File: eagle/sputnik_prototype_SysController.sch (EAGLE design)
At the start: 23 parts, among them U1 MEGA128-M, U2 MIC5219 3.3V, Y2 8MHZ

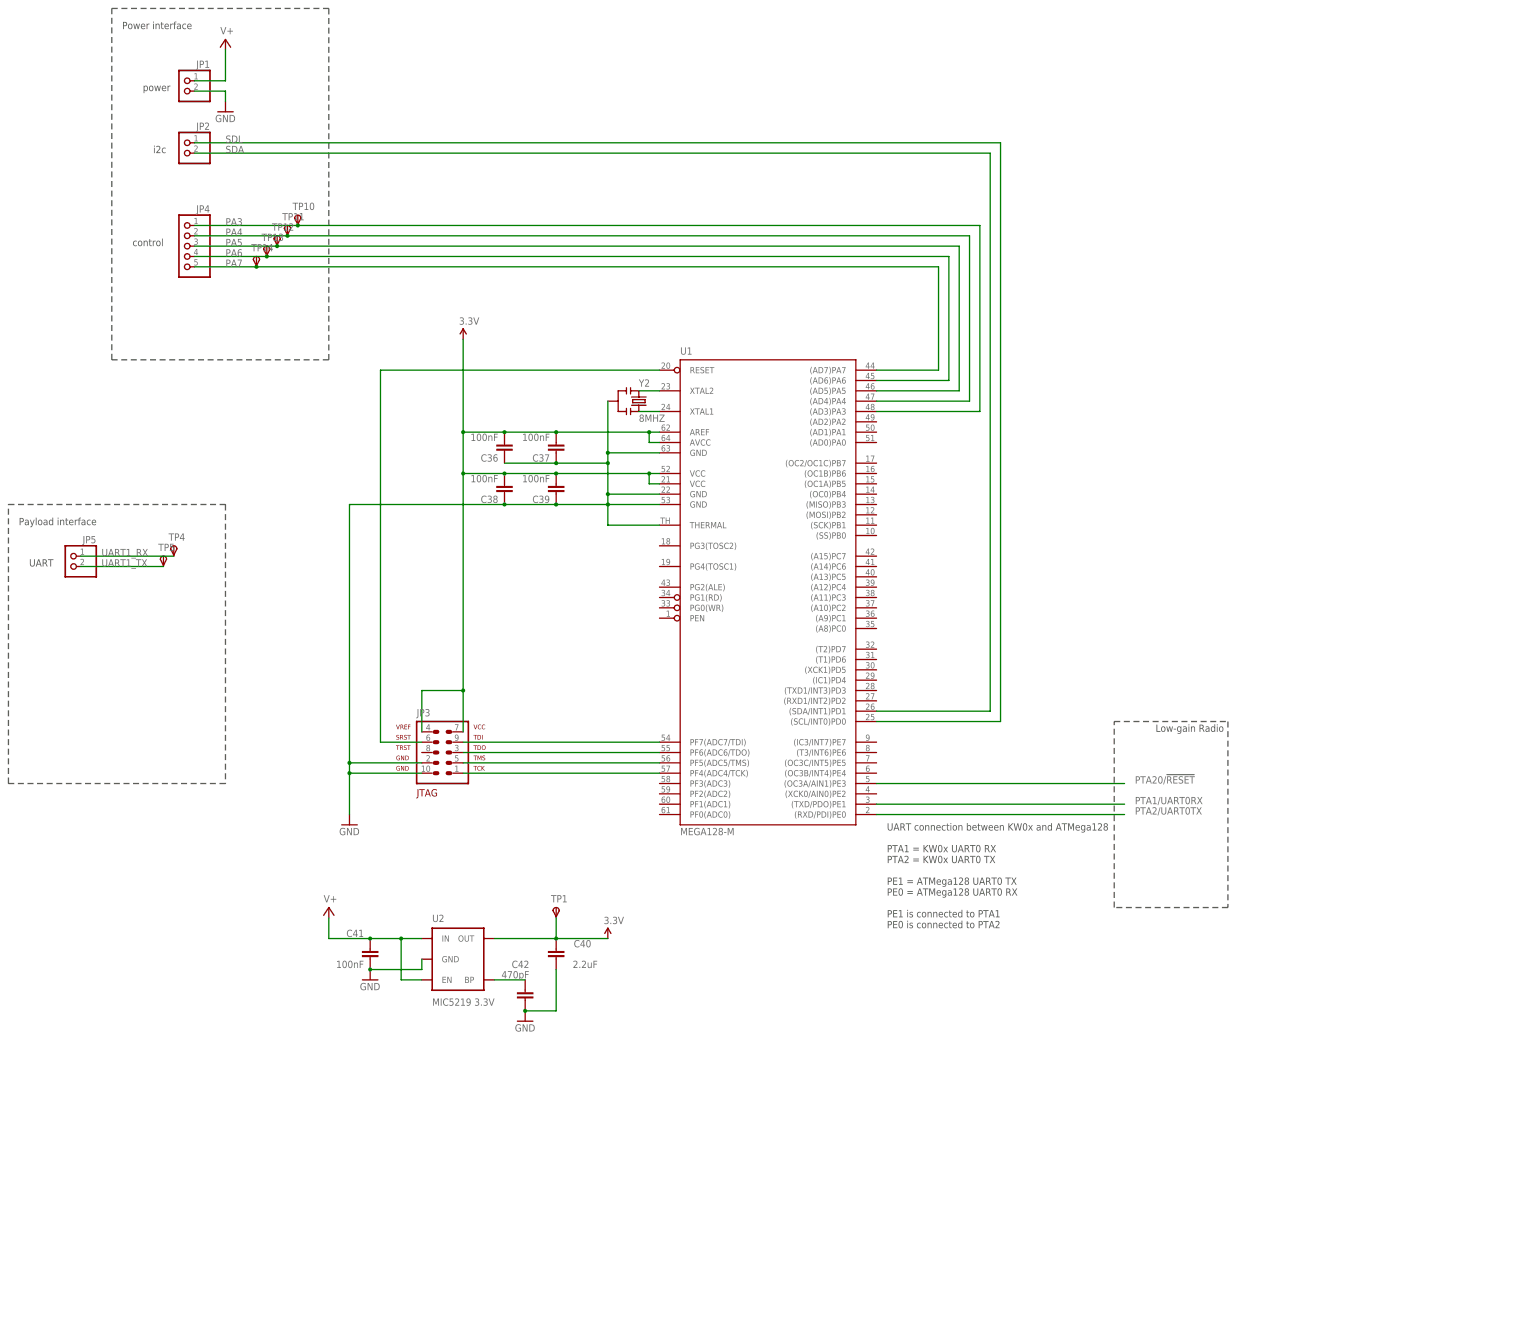
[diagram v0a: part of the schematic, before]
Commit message: Added GPIOs and other updates on SysCon sch. Updated SPI cache footprint
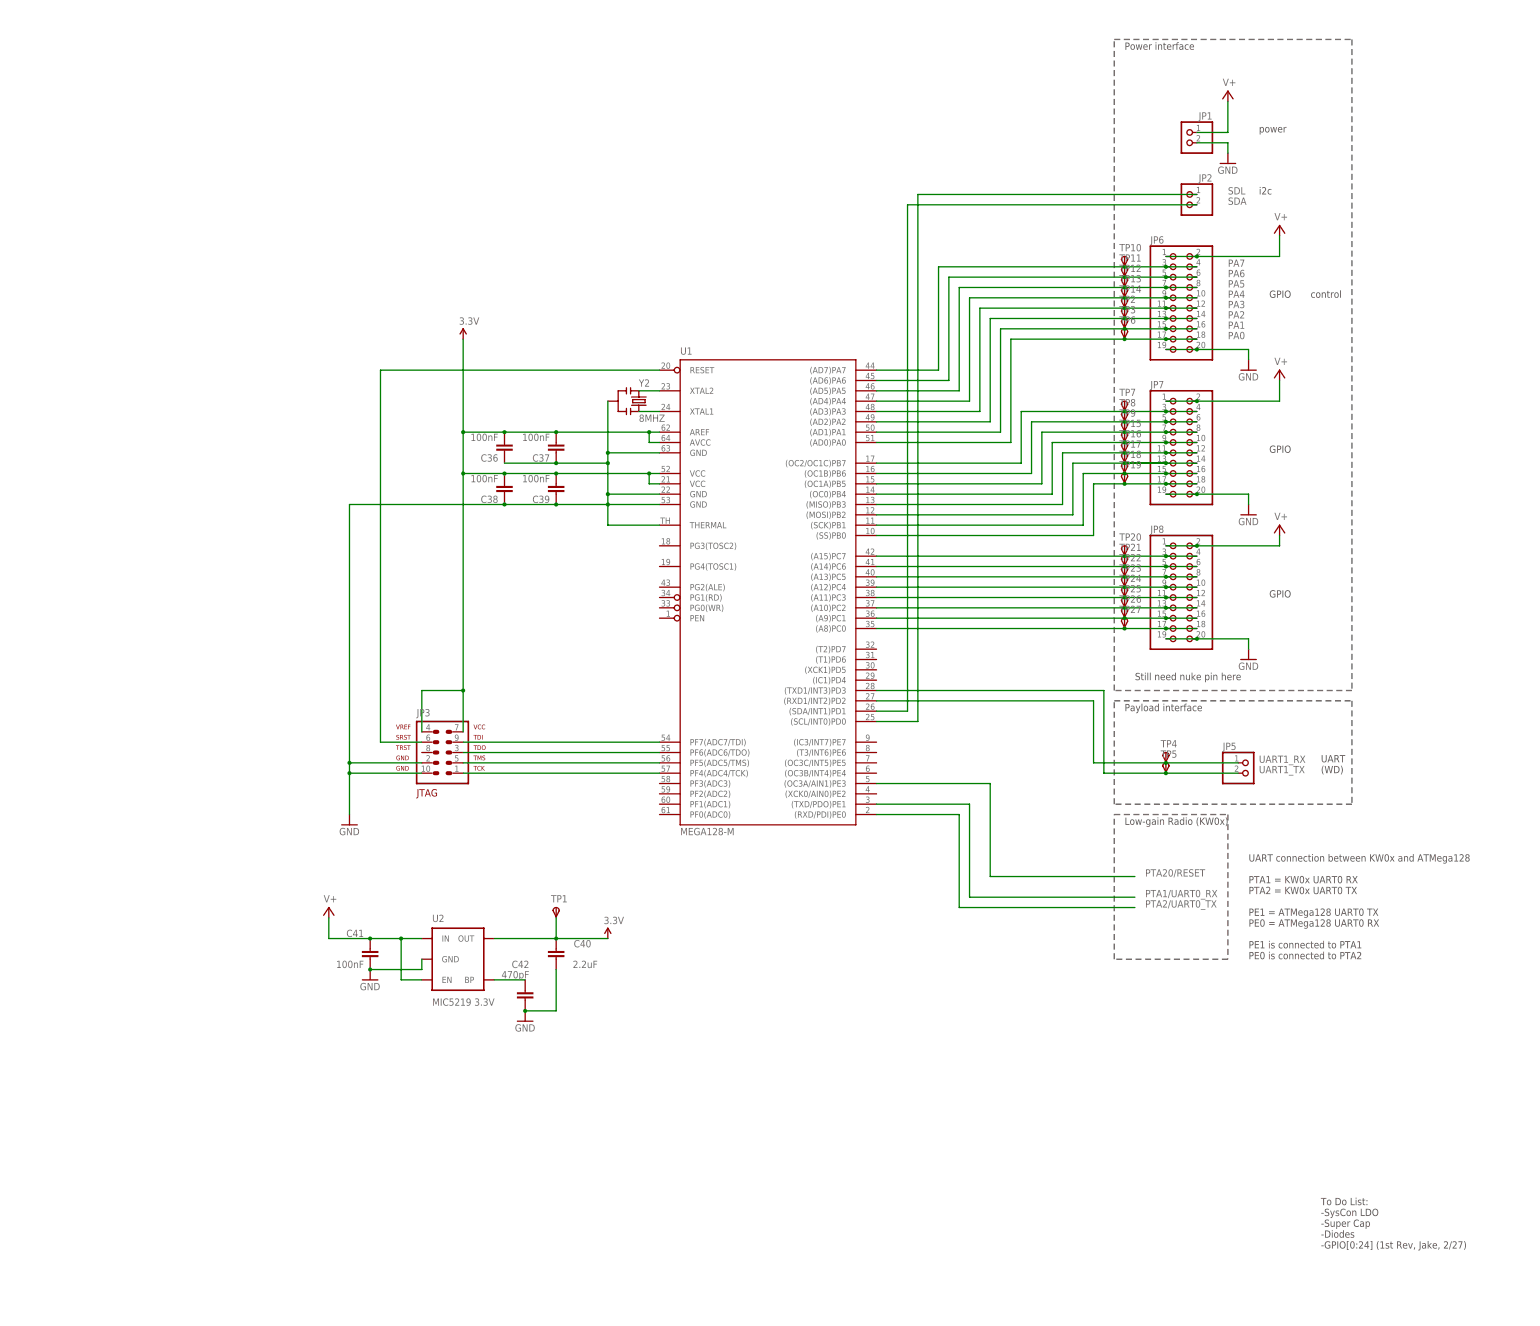
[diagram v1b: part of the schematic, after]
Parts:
- removed JP4: (no value), pinhead:PINHD-1X55X2MM
- added JP6, JP7, JP8: (no value), psas_c3_team05:PINHD-2X10
- added TP15, TP16, TP17, TP18, TP19, TP2, TP20, TP21, TP22, TP23, TP24, TP25, TP26, TP27, TP3, TP6, TP7, TP8, TP9: TPSPAD1-13, testpad:TPSPAD1-13
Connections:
- net PTA1/UART0RX renamed PTA1/UART0_RX
- net PTA2/UART0TX renamed PTA2/UART0_TX
- net PTA20/!RESET renamed PTA20/RESET
- new net PA0: JP6.17, JP6.18, TP6.PP, U1.(AD0)PA0
- new net PA1: JP6.15, JP6.16, TP3.PP, U1.(AD1)PA1
- new net PA2: JP6.13, JP6.14, TP2.PP, U1.(AD2)PA2
- new net PB0: JP7.17, JP7.18, TP19.PP, U1.(SS)PB0
- new net PB1: JP7.15, JP7.16, TP18.PP, U1.(SCK)PB1
- new net PB2: JP7.13, JP7.14, TP17.PP, U1.(MOSI)PB2
- new net PB3: JP7.11, JP7.12, TP16.PP, U1.(MISO)PB3
- new net PB4: JP7.10, JP7.9, TP15.PP, U1.(OC0)PB4
- new net PB5: JP7.7, JP7.8, TP9.PP, U1.(OC1A)PB5
- new net PB6: JP7.5, JP7.6, TP8.PP, U1.(OC1B)PB6
- new net PB7: JP7.3, JP7.4, TP7.PP, U1.(OC2/OC1C)PB7
- new net PC0: JP8.17, JP8.18, TP27.PP, U1.(A8)PC0
- new net PC1: JP8.15, JP8.16, TP26.PP, U1.(A9)PC1
- new net PC2: JP8.13, JP8.14, TP25.PP, U1.(A10)PC2
- new net PC3: JP8.11, JP8.12, TP24.PP, U1.(A11)PC3
- new net PC4: JP8.10, JP8.9, TP23.PP, U1.(A12)PC4
- new net PC5: JP8.7, JP8.8, TP22.PP, U1.(A13)PC5
- new net PC6: JP8.5, JP8.6, TP21.PP, U1.(A14)PC6
- new net PC7: JP8.3, JP8.4, TP20.PP, U1.(A15)PC7
- net GND: now also JP6.19, JP6.20, JP7.19, JP7.20, JP8.19, JP8.20
- net PA3: now also JP6.11, JP6.12, TP14.PP; no longer JP4.1, TP10.PP
- net PA4: now also JP6.10, JP6.9, TP13.PP; no longer JP4.2, TP11.PP
- net PA5: now also JP6.7, JP6.8; no longer JP4.3
- net PA6: now also JP6.5, JP6.6, TP11.PP; no longer JP4.4, TP13.PP
- net PA7: now also JP6.3, JP6.4, TP10.PP; no longer JP4.5, TP14.PP
- net UART1_RX: now also U1.(RXD1/INT2)PD2
- net UART1_TX: now also U1.(TXD1/INT3)PD3
- net V+: now also JP6.1, JP6.2, JP7.1, JP7.2, JP8.1, JP8.2
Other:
- note added: "GPIO"
- note added: "Low-gain Radio (KW0x)"
- note added: "Still need nuke pin here"
- note added: "To Do List: -SysCon LDO -Super Cap -Diodes -GPIO[0:24] (1st Rev, Jake, 2/27)"
- note added: "UART (WD)"
- note removed: "Low-gain Radio"
- note removed: "UART"
- moved on the sheet: JP1, JP2, JP5, TP10, TP11, TP12, TP13, TP14, TP4, TP5

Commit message: Added super cap and LDO holding place
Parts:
- added C1: CAP-ELNA-DS, cap-elna-ds:CAP-ELNA-DS
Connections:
- net 3.3V: now also C1.+
- net GND: now also C1.-
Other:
- note added: "LDO goes here"
- note added: "To Do List: -SysCon LDO -Super Cap (footprint & symbol, Jake, 2/27) -Diodes -GPIO[0:24] (1st Rev, Jake, 2/27)"
- note removed: "To Do List: -SysCon LDO -Super Cap -Diodes -GPIO[0:24] (1st Rev, Jake, 2/27)"
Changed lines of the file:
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@@
 <layer number="56" name="wert" color="7" fill="1" visible="no" active="no"/>
 <layer number="57" name="tCAD" color="7" fill="1" visible="no" active="no"/>
+<layer number="59" name="Invisible" color="7" fill="1" visible="no" active="no"/>
+<layer number="61" name="stand" color="7" fill="1" visible="no" active="no"/>
 <layer number="90" name="Modules" color="5" fill="1" visible="yes" active="yes"/>
 <layer number="91" name="Nets" color="2" fill="1" visible="yes" active="yes"/>
@@
 <layer number="127" name="_tValues" color="7" fill="1" visible="yes" active="yes"/>
 <layer number="128" name="_bValues" color="7" fill="1" visible="yes" active="yes"/>
+<layer number="130" name="bLogo" color="7" fill="1" visible="yes" active="yes"/>
 <layer number="131" name="tAdjust" color="7" fill="1" visible="yes" active="yes"/>
 <layer number="132" name="bAdjust" color="7" fill="1" visible="yes" active="yes"/>
@@
 <layer number="223" name="223bmp" color="7" fill="1" visible="yes" active="yes"/>
 <layer number="224" name="224bmp" color="7" fill="1" visible="yes" active="yes"/>
+<layer number="225" name="225bmp" color="7" fill="1" visible="yes" active="yes"/>
+<layer number="226" name="226bmp" color="7" fill="1" visible="yes" active="yes"/>
+<layer number="227" name="227bmp" color="7" fill="1" visible="yes" active="yes"/>
+<layer number="228" name="228bmp" color="7" fill="1" visible="yes" active="yes"/>
 <layer number="231" name="Eagle3D_PG1" color="7" fill="1" visible="yes" active="yes"/>
 <layer number="232" name="Eagle3D_PG2" color="7" fill="1" visible="yes" active="yes"/>
@@
 <part name="TP26" library="testpad" deviceset="TPS" device="PAD1-13"/>
 <part name="TP27" library="testpad" deviceset="TPS" device="PAD1-13"/>
+<part name="C1" library="cap-elna-ds" deviceset="CAP-ELNA-DS" device=""/>
+<part name="GND6" library="psas_c3_team05" deviceset="GND" device=""/>
 </parts>
 <sheets>
@@
 <text x="444.5" y="53.34" size="1.778" layer="97">To Do List:
 -SysCon LDO
--Super Cap
+-Super Cap (footprint &amp; symbol, Jake, 2/27)
 -Diodes
 -GPIO[0:24] (1st Rev, Jake, 2/27)</text>
@@
 <text x="431.8" y="213.36" size="1.778" layer="97">GPIO</text>
 <text x="398.78" y="193.04" size="1.778" layer="97">Still need nuke pin here</text>
+<wire x1="167.64" y1="317.5" x2="213.36" y2="317.5" width="0.1524" layer="97" style="longdash"/>
+<wire x1="213.36" y1="317.5" x2="213.36" y2="274.32" width="0.1524" layer="97" style="longdash"/>
+<wire x1="213.36" y1="274.32" x2="167.64" y2="274.32" width="0.1524" layer="97" style="longdash"/>
+<wire x1="167.64" y1="274.32" x2="167.64" y2="317.5" width="0.1524" layer="97" style="longdash"/>
+<text x="170.18" y="314.96" size="1.778" layer="97">LDO goes here</text>
 </plain>
 <instances>
@@
 <instance part="TP13" gate="G$1" x="396.24" y="289.56"/>
 <instance part="TP14" gate="G$1" x="396.24" y="287.02"/>
-<instance part="P+5" gate="G$1" x="233.68" y="276.86"/>
+<instance part="P+5" gate="G$1" x="111.76" y="292.1"/>
 <instance part="C40" gate="CE" x="256.54" y="124.46" smashed="yes" rot="R180">
 <attribute name="NAME" x="265.176" y="129.159" size="1.778" layer="95" rot="R180"/>
@@
 <instance part="TP26" gate="G$1" x="396.24" y="210.82"/>
 <instance part="TP27" gate="G$1" x="396.24" y="208.28"/>
+<instance part="C1" gate="G$1" x="149.86" y="279.4"/>
+<instance part="GND6" gate="1" x="149.86" y="269.24"/>
 </instances>
 <busses>
@@
 <junction x="414.02" y="274.32"/>
 </segment>
+<segment>
+<pinref part="C1" gate="G$1" pin="-"/>
+<pinref part="GND6" gate="1" pin="GND"/>
+<wire x1="149.86" y1="274.32" x2="149.86" y2="271.78" width="0.1524" layer="91"/>
+</segment>
 </net>
 <net name="V+" class="0">
@@
 </segment>
 <segment>
-<pinref part="JP3" gate="G$1" pin="7"/>
-<pinref part="JP3" gate="G$1" pin="4"/>
-<wire x1="233.68" y1="276.86" x2="233.68" y2="254" width="0.1524" layer="91"/>
+<pinref part="P+5" gate="G$1" pin="3.3V"/>
+<wire x1="111.76" y1="292.1" x2="111.76" y2="289.56" width="0.1524" layer="91"/>
+<wire x1="111.76" y1="289.56" x2="149.86" y2="289.56" width="0.1524" layer="91"/>
+<wire x1="149.86" y1="289.56" x2="233.68" y2="289.56" width="0.1524" layer="91"/>
 <wire x1="233.68" y1="254" x2="233.68" y2="243.84" width="0.1524" layer="91"/>
-<wire x1="233.68" y1="243.84" x2="233.68" y2="190.5" width="0.1524" layer="91"/>
-<wire x1="233.68" y1="190.5" x2="233.68" y2="180.34" width="0.1524" layer="91"/>
-<wire x1="223.52" y1="180.34" x2="223.52" y2="190.5" width="0.1524" layer="91"/>
-<wire x1="223.52" y1="190.5" x2="233.68" y2="190.5" width="0.1524" layer="91"/>
-<junction x="233.68" y="190.5"/>
 <pinref part="C36" gate="CE" pin="2"/>
 <wire x1="233.68" y1="254" x2="243.84" y2="254" width="0.1524" layer="91"/>
-<junction x="233.68" y="254"/>
 <pinref part="C37" gate="CE" pin="2"/>
 <wire x1="243.84" y1="254" x2="256.54" y2="254" width="0.1524" layer="91"/>
@@
 <pinref part="C38" gate="CE" pin="2"/>
 <wire x1="233.68" y1="243.84" x2="243.84" y2="243.84" width="0.1524" layer="91"/>
-<junction x="233.68" y="243.84"/>
 <pinref part="C39" gate="CE" pin="2"/>
 <wire x1="243.84" y1="243.84" x2="256.54" y2="243.84" width="0.1524" layer="91"/>
@@
 <wire x1="279.4" y1="241.3" x2="279.4" y2="243.84" width="0.1524" layer="91"/>
 <junction x="279.4" y="243.84"/>
-<pinref part="P+5" gate="G$1" pin="3.3V"/>
-</segment>
-</net>
+<wire x1="233.68" y1="289.56" x2="233.68" y2="254" width="0.1524" layer="91"/>
+<junction x="233.68" y="254"/>
+<pinref part="JP3" gate="G$1" pin="7"/>
+<wire x1="233.68" y1="190.5" x2="233.68" y2="180.34" width="0.1524" layer="91"/>
+<wire x1="223.52" y1="190.5" x2="233.68" y2="190.5" width="0.1524" layer="91"/>
+<pinref part="JP3" gate="G$1" pin="4"/>
+<wire x1="223.52" y1="180.34" x2="223.52" y2="190.5" width="0.1524" layer="91"/>
+<wire x1="233.68" y1="243.84" x2="233.68" y2="190.5" width="0.1524" layer="91"/>
+<junction x="233.68" y="243.84"/>
+<junction x="233.68" y="190.5"/>
+<pinref part="C1" gate="G$1" pin="+"/>
+<wire x1="149.86" y1="284.48" x2="149.86" y2="289.56" width="0.1524" layer="91"/>
+<junction x="149.86" y="289.56"/>
+</segment>
+</net>
